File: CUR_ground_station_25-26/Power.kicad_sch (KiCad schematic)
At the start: 0 parts

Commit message: added power stuff
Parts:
- added C28, C29: 1u, Capacitor_SMD:C_0603_1608Metric, symbol Device:C_Small
- added J?: Conn_01x02_Pin, symbol Connector:Conn_01x02_Pin
- added R10, R11: 10k, Resistor_SMD:R_0603_1608Metric, symbol Device:R_Small_US
- added U6: BU33SD5, BUxxSD5:SSOP5_ROM, symbol BUxxSD5:BU33SD5
- added U7: LM66200, Package_TO_SOT_SMD:SOT-583-8, symbol LM66200:LM66200
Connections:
- new net: R10.2, U7.4 (~{ON})
- new net +3V3: C29.1, R11.2, U6.5 (VOUT)
- new net +BATT: U7.6 (VIN2)
- new net GND: C28.2, C29.2, J?.1 (Pin_1), R10.1, U6.2 (GND), U7.1 (GND), U7.5 (GND)
- new net LDO_IN: C28.1, U6.1 (VIN), U6.3 (STDBY), U7.2 (VOUT), U7.7 (VOUT)
- new net LM660_ST: U7.8 (ST)
- new net VBUS: U7.3 (VIN1)
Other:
- note added: "Linear Regulator 3.3V"
- note added: "Switching IC will switch to usb power if plugged in"

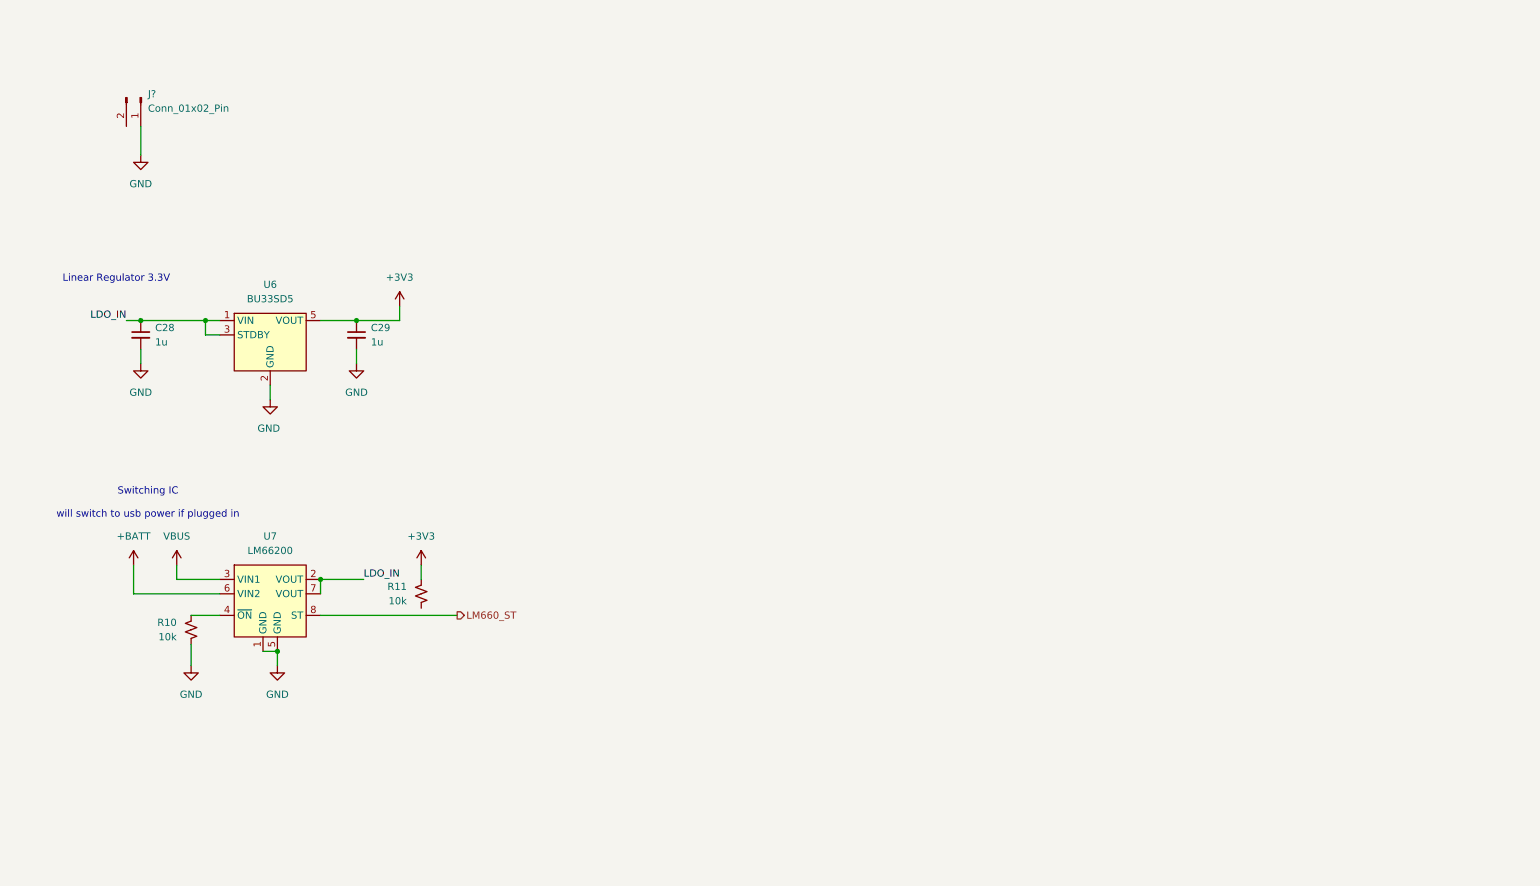
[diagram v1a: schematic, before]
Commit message: Implement battery management, soft power on, and LDO
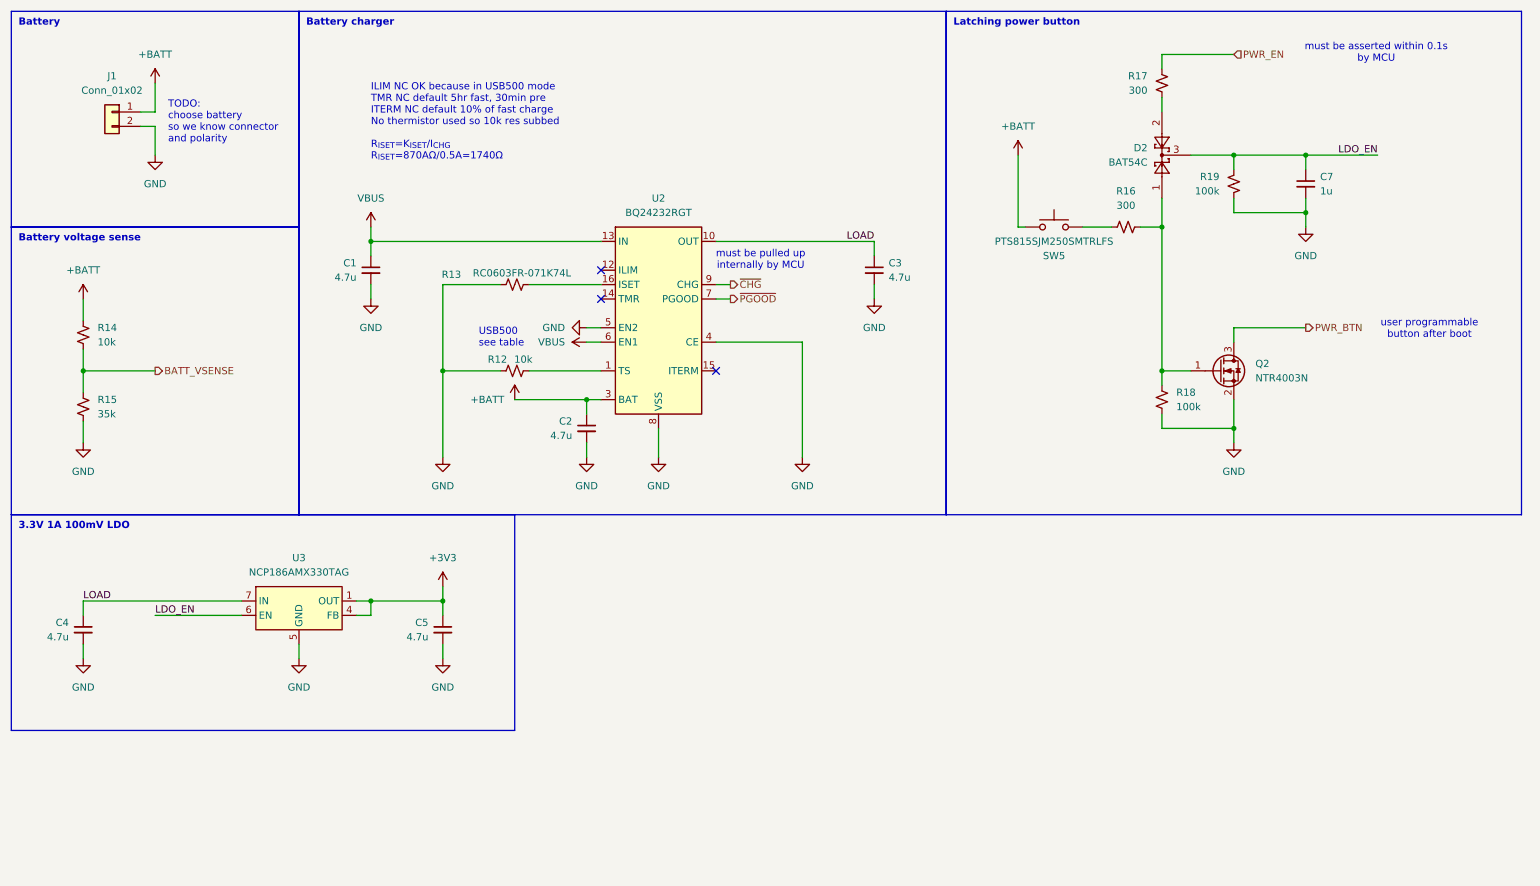
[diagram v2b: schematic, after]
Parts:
- removed C28, C29: 1u, Capacitor_SMD:C_0603_1608Metric, symbol Device:C_Small
- removed J?: Conn_01x02_Pin, symbol Connector:Conn_01x02_Pin
- removed R10, R11: 10k, Resistor_SMD:R_0603_1608Metric, symbol Device:R_Small_US
- removed U6: BU33SD5, BUxxSD5:SSOP5_ROM, symbol BUxxSD5:BU33SD5
- removed U7: LM66200, Package_TO_SOT_SMD:SOT-583-8, symbol LM66200:LM66200
- added C1, C2, C3, C4, C5: 4.7u, symbol Device:C_Small
- added C7: 1u, Capacitor_SMD:C_0402_1005Metric, symbol Device:C_Small
- added D2: BAT54C, Package_TO_SOT_SMD:SOT-23, symbol Diode:BAT54C
- added J1: Conn_01x02, symbol Connector_Generic:Conn_01x02
- added Q2: NTR4003N, Package_TO_SOT_SMD:SOT-23, symbol Transistor_FET:Q_NMOS_GSD
- added R12, R14: 10k, symbol Device:R_Small_US
- added R13: RC0603FR-071K74L, symbol Device:R_Small_US
- added R15: 35k, symbol Device:R_Small_US
- added R16, R17: 300, Resistor_SMD:R_0402_1005Metric, symbol Device:R_Small_US
- added R18, R19: 100k, Resistor_SMD:R_0402_1005Metric, symbol Device:R_Small_US
- added SW5: PTS815SJM250SMTRLFS, PTS815_SJM_250_SMTR_LFS:SW_Push_PTS815_SJM_250_SMTR_LFS, symbol Switch:SW_Push
- added U2: BQ24232RGT, Package_DFN_QFN:VQFN-16-1EP_3x3mm_P0.5mm_EP1.68x1.68mm_ThermalVias, symbol TI_Battery_Management:BQ24232RGT
- added U3: NCP186AMX330TAG, Package_DFN_QFN:DFN-6-1EP_1.2x1.2mm_P0.4mm_EP0.3x0.94mm_PullBack, symbol Regulator_Linear_onsemi:NCP186AMX330TAG
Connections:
- net +3V3: now also C5.1, U3.1 (OUT), U3.2 (OUT), U3.4 (FB)
- net +BATT: now also C2.1, J1.1 (Pin_1), R14.1, SW5.1, U2.2 (BAT), U2.3 (BAT)
- net GND: now also C1.2, C2.2, C3.2, C4.2, C5.2, C7.2, J1.2 (Pin_2), Q2.2 (S), R12.1, R13.1, R15.2, R18.2, R19.2, U2.17 (VSS), U2.4 (CE), U2.5 (EN2), U2.8 (VSS), U3.3 (N/C), U3.5 (GND), U3.9 (EPAD)
- net VBUS: now also C1.1, U2.13 (IN), U2.6 (EN1)
- new net: R12.2, U2.1 (TS)
- new net: R13.2, U2.16 (ISET)
- new net: D2.1, Q2.1 (G), R16.2, R18.1
- new net: D2.2, R17.2
- new net: R16.1, SW5.2
- new net BATT_VSENSE: R14.2, R15.1
- new net IN: C3.1, C4.1, U2.10 (OUT), U2.11 (OUT), U3.7 (IN), U3.8 (IN)
- new net LDO_EN: C7.1, D2.3, R19.1, U3.6 (EN)
- new net PWR_BTN: Q2.3 (D)
- new net PWR_EN: R17.1
- new net ~{CHG}: U2.9 (CHG)
- new net ~{PGOOD}: U2.7 (PGOOD)
- no-connect marks 0 -> 3
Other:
- note added: "3.3V 1A 100mV LDO"
- note added: "Battery"
- note added: "Battery charger"
- note added: "Battery voltage sense"
- note added: "ILIM NC OK because in USB500 mode TMR NC default 5hr fast, 30min pre ITERM NC default 10% of fast charge No thermistor used so 10k res subbed"
- note added: "Latching power button"
- note added: "R_{ISET}=K_{ISET}/I_{CHG} R_{ISET}=870AΩ/0.5A=1740Ω"
- note added: "TODO: choose battery so we know connector and polarity"
- note added: "USB500 see table"
- note added: "must be asserted within 0.1s by MCU"
- note added: "must be pulled up internally by MCU"
- note added: "user programmable button after boot"
- note removed: "Linear Regulator 3.3V"
- note removed: "Switching IC will switch to usb power if plugged in"

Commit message: added buncha stuff from flight computer
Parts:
- added D3: LED, LED_SMD:LED_0603_1608Metric, symbol Device:LED
- added J2: UJ20-C-H-G-SMT-P16-TR, SAMESKY_UJ20-C-H-G-SMT-P16-TR:SAMESKY_UJ20-C-H-G-SMT-P16-TR, symbol Connector:USB_C_Receptacle_USB2.0_16P
- added R20, R21: 5.1k, Resistor_SMD:R_0603_1608Metric, symbol Device:R_Small_US
- added R22: 150, Resistor_SMD:R_0603_1608Metric, symbol Device:R_Small_US
- added U4: USBLC6-2SC6, Package_TO_SOT_SMD:SOT-23-6, symbol Power_Protection:USBLC6-2SC6
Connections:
- net +3V3: now also R22.2
- net GND: now also D3.1 (K), J2.A1 (GND), J2.A12 (GND), J2.B1 (GND), J2.B12 (GND), J2.S1 (SHIELD), R20.2, R21.2, U4.2 (GND)
- net VBUS: now also J2.A4 (VBUS), J2.A9 (VBUS), J2.B4 (VBUS), J2.B9 (VBUS), U4.5 (VBUS)
- new net: J2.A5 (CC1), R20.1
- new net: J2.A6 (D+), J2.B6 (D+), U4.3 (I/O2)
- new net: J2.A7 (D-), J2.B7 (D-), U4.1 (I/O1)
- new net: J2.B5 (CC2), R21.1
- new net: D3.2 (A), R22.1
- new net USB_D+: U4.4 (I/O2)
- new net USB_D-: U4.6 (I/O1)
- no-connect marks 3 -> 5
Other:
- note added: "Battery Indicator"
- note added: "ESD protection place close to connector"
- note added: "USB-C connector"

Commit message: Correct soft power off circuit to support USB and battery
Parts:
- added D4: BAT54C, Package_TO_SOT_SMD:SOT-23, symbol Diode:BAT54C
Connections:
- net +BATT: now also D4.2; no longer SW5.1
- net VBUS: now also D4.1
- new net: D4.3, SW5.1
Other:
- note added: "Power Indicator"
- note removed: "Battery Indicator"
- moved on the sheet: R16, SW5
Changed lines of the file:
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@@
 		)
 	)
-	(text "Battery Indicator\n"
+	(text "Power Indicator"
 		(exclude_from_sim no)
 		(at 104.394 103.886 0)
@@
 	(wire
 		(pts
+			(xy 181.61 40.64) (xy 181.61 60.96)
+		)
+		(stroke
+			(width 0)
+			(type default)
+		)
+	)
+	(wire
+		(pts
 			(xy 217.17 133.35) (xy 217.17 135.89)
 		)
@@
 	(wire
 		(pts
-			(xy 212.09 50.8) (xy 215.9 50.8)
+			(xy 213.36 50.8) (xy 215.9 50.8)
 		)
 		(stroke
@@
 	(wire
 		(pts
-			(xy 201.93 50.8) (xy 207.01 50.8)
+			(xy 205.74 50.8) (xy 208.28 50.8)
 		)
 		(stroke
@@
 	(wire
 		(pts
+			(xy 187.96 40.64) (xy 187.96 43.18)
+		)
+		(stroke
+			(width 0)
+			(type default)
+		)
+	)
+	(wire
+		(pts
 			(xy 38.1 38.1) (xy 38.1 33.02)
 		)
@@
 	(wire
 		(pts
-			(xy 190.5 38.1) (xy 190.5 50.8)
+			(xy 76.2 50.8) (xy 76.2 53.34)
 		)
 		(stroke
@@
 	(wire
 		(pts
-			(xy 76.2 50.8) (xy 76.2 53.34)
+			(xy 114.3 88.9) (xy 114.3 91.44)
 		)
 		(stroke
@@
 	(wire
 		(pts
-			(xy 114.3 88.9) (xy 114.3 91.44)
+			(xy 217.17 133.35) (xy 247.65 133.35)
 		)
 		(stroke
@@
 	(wire
 		(pts
-			(xy 217.17 133.35) (xy 247.65 133.35)
+			(xy 215.9 50.8) (xy 215.9 76.2)
 		)
 		(stroke
@@
 	(wire
 		(pts
-			(xy 215.9 50.8) (xy 215.9 76.2)
+			(xy 187.96 60.96) (xy 187.96 58.42)
 		)
 		(stroke
@@
 		)
 	)
+	(wire
+		(pts
+			(xy 181.61 60.96) (xy 187.96 60.96)
+		)
+		(stroke
+			(width 0)
+			(type default)
+		)
+	)
 	(polyline
 		(pts
@@
 	(wire
 		(pts
-			(xy 190.5 50.8) (xy 191.77 50.8)
+			(xy 193.04 50.8) (xy 195.58 50.8)
 		)
 		(stroke
@@
 	(symbol
 		(lib_id "power:+BATT")
-		(at 190.5 38.1 0)
+		(at 187.96 40.64 0)
 		(unit 1)
 		(exclude_from_sim no)
@@
 		(fields_autoplaced yes)
 		(property "Reference" "#PWR028"
-			(at 190.5 41.91 0)
+			(at 187.96 44.45 0)
 			(effects
 				(font
@@
 		)
 		(property "Value" "+BATT"
-			(at 190.5 33.02 0)
+			(at 187.96 35.56 0)
 			(effects
 				(font
@@
 		)
 		(property "Footprint" ""
-			(at 190.5 38.1 0)
+			(at 187.96 40.64 0)
 			(effects
 				(font
@@
 		)
 		(property "Datasheet" ""
-			(at 190.5 38.1 0)
+			(at 187.96 40.64 0)
 			(effects
 				(font
@@
 		)
 		(property "Description" "Power symbol creates a global label with name \"+BATT\""
-			(at 190.5 38.1 0)
+			(at 187.96 40.64 0)
 			(effects
 				(font
@@
 	(symbol
 		(lib_id "power:VBUS")
+		(at 181.61 40.64 0)
+		(unit 1)
+		(exclude_from_sim no)
+		(in_bom yes)
+		(on_board yes)
+		(dnp no)
+		(fields_autoplaced yes)
+		(property "Reference" "#PWR043"
+			(at 181.61 44.45 0)
+			(effects
+				(font
+					(size 1.27 1.27)
+				)
+				(hide yes)
+			)
+		)
+		(property "Value" "VBUS"
+			(at 181.61 35.56 0)
+			(effects
+				(font
+					(size 1.27 1.27)
+				)
+			)
+		)
+		(property "Footprint" ""
+			(at 181.61 40.64 0)
+			(effects
+				(font
+					(size 1.27 1.27)
+				)
+				(hide yes)
+			)
+		)
+		(property "Datasheet" ""
+			(at 181.61 40.64 0)
+			(effects
+				(font
+					(size 1.27 1.27)
+				)
+				(hide yes)
+			)
+		)
+		(property "Description" "Power symbol creates a global label with name \"VBUS\""
+			(at 181.61 40.64 0)
+			(effects
+				(font
+					(size 1.27 1.27)
+				)
+				(hide yes)
+			)
+		)
+		(pin "1"
+		)
+		(instances
+			(project ""
+				(path "/b6f682bd-f29b-4650-adb4-b230be0368ad/81c93bb2-d3b4-4976-ae9e-2e07f946e0a4"
+					(reference "#PWR043")
+					(unit 1)
+				)
+			)
+		)
+	)
+	(symbol
+		(lib_id "power:VBUS")
 		(at 114.3 71.12 90)
 		(unit 1)
@@
 	)
 	(symbol
+		(lib_id "Diode:BAT54C")
+		(at 187.96 50.8 90)
+		(unit 1)
+		(exclude_from_sim no)
+		(in_bom yes)
+		(on_board yes)
+		(dnp no)
+		(property "Reference" "D4"
+			(at 185.42 49.5299 90)
+			(effects
+				(font
+					(size 1.27 1.27)
+				)
+				(justify left)
+			)
+		)
+		(property "Value" "BAT54C"
+			(at 185.42 52.0699 90)
+			(effects
+				(font
+					(size 1.27 1.27)
+				)
+				(justify left)
+			)
+		)
+		(property "Footprint" "Package_TO_SOT_SMD:SOT-23"
+			(at 184.785 48.895 0)
+			(effects
+				(font
+					(size 1.27 1.27)
+				)
+				(justify left)
+				(hide yes)
+			)
+		)
+		(property "Datasheet" "http://www.diodes.com/_files/datasheets/ds11005.pdf"
+			(at 187.96 52.832 0)
+			(effects
+				(font
+					(size 1.27 1.27)
+				)
+				(hide yes)
+			)
+		)
+		(property "Description" "dual schottky barrier diode, common cathode"
+			(at 187.96 50.8 0)
+			(effects
+				(font
+					(size 1.27 1.27)
+				)
+				(hide yes)
+			)
+		)
+		(property "HQ_MPN" "DS0140568"
+			(at 187.96 50.8 90)
+			(effects
+				(font
+					(size 1.27 1.27)
+				)
+				(hide yes)
+			)
+		)
+		(pin "3"
+		)
+		(pin "2"
+		)
+		(pin "1"
+		)
+		(instances
+			(project "CUR_ground_station_25-26"
+				(path "/b6f682bd-f29b-4650-adb4-b230be0368ad/81c93bb2-d3b4-4976-ae9e-2e07f946e0a4"
+					(reference "D4")
+					(unit 1)
+				)
+			)
+		)
+	)
+	(symbol
 		(lib_id "Device:R_Small_US")
 		(at 215.9 25.4 0)
@@
 	(symbol
 		(lib_id "Switch:SW_Push")
-		(at 196.85 50.8 0)
+		(at 200.66 50.8 0)
 		(unit 1)
 		(exclude_from_sim no)
@@
 		(dnp no)
 		(property "Reference" "SW5"
-			(at 196.85 55.88 0)
+			(at 200.66 55.88 0)
 			(effects
 				(font
@@
 		)
 		(property "Value" "PTS815SJM250SMTRLFS"
-			(at 196.85 53.34 0)
+			(at 200.66 53.34 0)
 			(effects
 				(font
@@
 		)
 		(property "Footprint" "PTS815_SJM_250_SMTR_LFS:SW_Push_PTS815_SJM_250_SMTR_LFS"
-			(at 196.85 45.72 0)
+			(at 200.66 45.72 0)
 			(effects
 				(font
@@
 		)
 		(property "Datasheet" "~"
-			(at 196.85 45.72 0)
+			(at 200.66 45.72 0)
 			(effects
 				(font
@@
 		)
 		(property "Description" "Push button switch, generic, two pins"
-			(at 196.85 50.8 0)
+			(at 200.66 50.8 0)
 			(effects
 				(font
@@
 		)
 		(property "HQ_MPN" "SKRPADE010"
-			(at 196.85 50.8 0)
+			(at 200.66 50.8 0)
 			(effects
 				(font
@@
 	(symbol
 		(lib_id "Device:R_Small_US")
-		(at 209.55 50.8 90)
+		(at 210.82 50.8 90)
 		(unit 1)
 		(exclude_from_sim no)
@@
 		(fields_autoplaced yes)
 		(property "Reference" "R16"
-			(at 209.55 44.45 90)
+			(at 210.82 44.45 90)
 			(effects
 				(font
@@
 		)
 		(property "Value" "300"
-			(at 209.55 46.99 90)
+			(at 210.82 46.99 90)
 			(effects
 				(font
@@
 		)
 		(property "Footprint" "Resistor_SMD:R_0402_1005Metric"
-			(at 209.55 50.8 0)
+			(at 210.82 50.8 0)
 			(effects
 				(font
@@
 		)
 		(property "Datasheet" "~"
-			(at 209.55 50.8 0)
+			(at 210.82 50.8 0)
 			(effects
 				(font
@@
 		)
 		(property "Description" "Resistor, small US symbol"
-			(at 209.55 50.8 0)
+			(at 210.82 50.8 0)
 			(effects
 				(font
@@
 		)
 		(property "HQ_MPN" "RTT02301JTH"
-			(at 209.55 50.8 90)
+			(at 210.82 50.8 90)
 			(effects
 				(font
